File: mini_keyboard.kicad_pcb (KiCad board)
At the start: 2 copper layers, 148.6 x 96.5 mm, 47 parts, among them J1 Conn_01x05_Male, SW1 SW_DIP_x01, SW10 SW_DIP_x01, SW11 SW_DIP_x01, SW12 SW_DIP_x01, SW13 SW_DIP_x01, SW14 SW_DIP_x01, SW15 SW_DIP_x01, SW16 SW_DIP_x01, SW17 SW_DIP_x01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

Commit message: Cleaned up no cables
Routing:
- net /out4: track 178.8 -> 165.7 mm

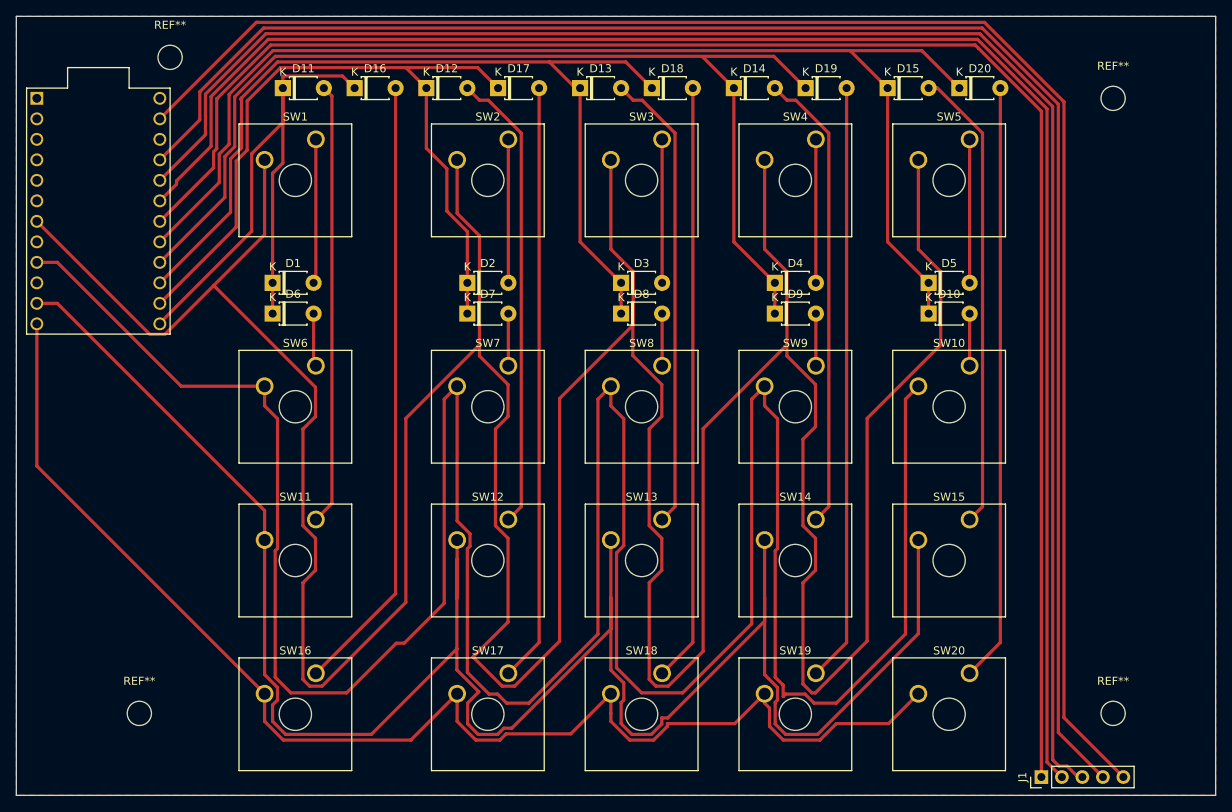
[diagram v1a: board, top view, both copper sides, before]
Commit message: B.Cu as main layer. red swapped to green
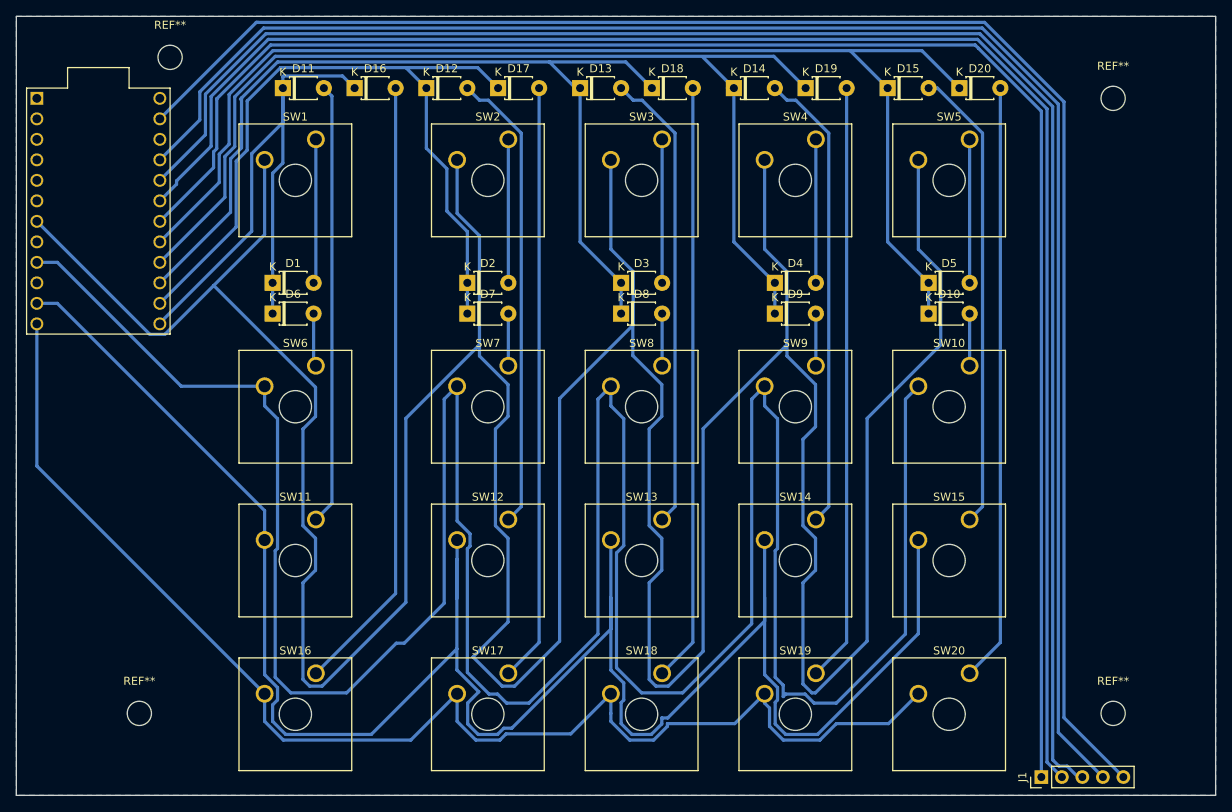
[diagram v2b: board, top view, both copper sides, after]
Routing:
- added copper zone on B.Cu, net (none)
- removed copper zone on F.Cu, net (none)
